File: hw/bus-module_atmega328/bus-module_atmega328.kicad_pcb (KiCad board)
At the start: 2 copper layers, 35 x 48 mm, 31 parts, among them J1 CONN_10X2, J2 CONN_7X2, J3 CONN-ISP-6, J5 CONN_1, J6 CONN_1, J7 CONN_1, J8 CONN_1, U1 ATMEGA328-TQFP32, U2 7,3728MHz, U3 25LC256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

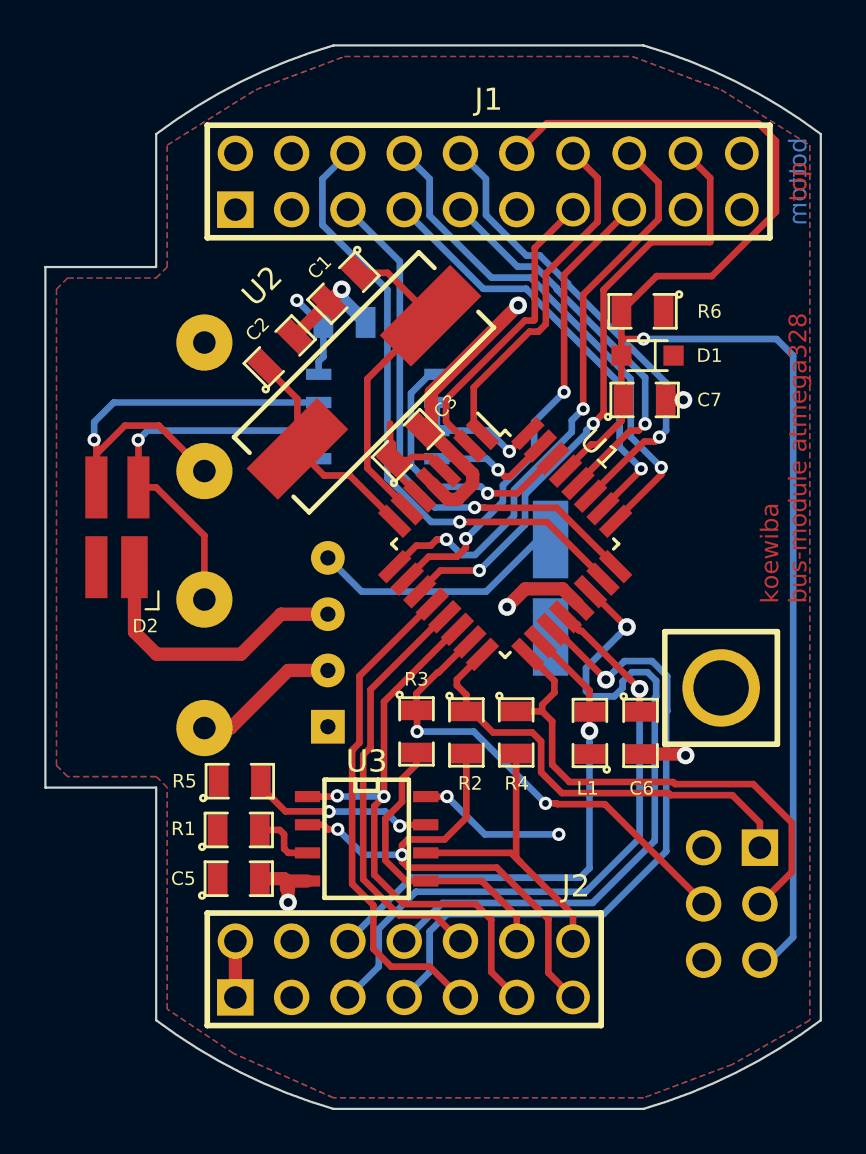
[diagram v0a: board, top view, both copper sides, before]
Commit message: bus-module_atmega328 update to rev B
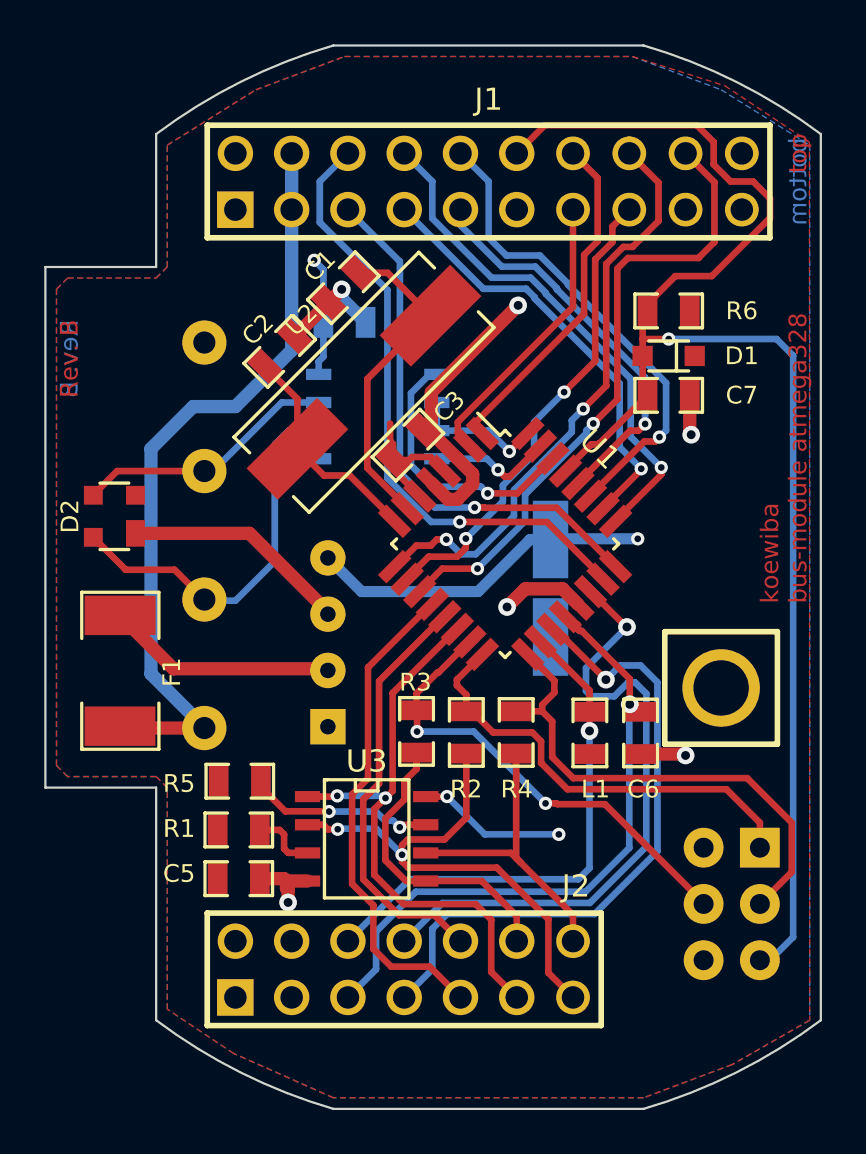
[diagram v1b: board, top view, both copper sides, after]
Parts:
- added F1: FUSE, Resistor:R_1812, F.Cu at (83.4, 104.2)
- C1, C2, C3, C5, C6, C7, C8: footprint Housings_SOIC:SM0805 -> Capacitors_SMD:C_0805
- C9: footprint Capacitors:cp_smd_6.3 -> Capacitors_SMD:CP_D6.3mm
- D1: footprint Diode:SOD323 -> Diode_SMD:D_SOD323
- D2: footprint Housings_SOT:SOT143R_Diode_Reverse -> Diode_SMD:D_SOT143
- J5, J6, J7, J8: footprint Connector_Miscelleaneus:WAGO243 -> Connector_WAGO:WAGO243
- L1: footprint Housings_SOIC:SM0805 -> Inductor:L_0805
- R1, R2, R3, R4, R5, R6: footprint Housings_SOIC:SM0805 -> Resistor:R_0805
- U2: footprint Crystal:HC49-SMD -> Crystal:CRY_HC49_SMD
- moved R6 1.18 mm to (108.1, 88.0)
- moved C7 1.11 mm to (108.1, 91.8)
- moved D1 0.96 mm to (108.1, 90.0)
- moved D2 0.52 mm to (83.1, 97.3), turned to 90 degrees
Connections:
- J1 pad 3: VCC -> +24V
- J1 pad 4: VCC -> +24V
- U5 pad 2: +24V -> Net-(F1-Pad1)
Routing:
- net +24V: track 6.65 -> 34.6 mm
- net Net-(F1-Pad1): track 0.00 -> 10.5 mm
- net /B: track 21.4 -> 11.9 mm, vias 1 -> 0
- net VCC: track 28.4 -> 34.4 mm, vias 3 -> 4
- net GND: track 44.2 -> 39.5 mm
- net //RESET: track 68.9 -> 66.6 mm
- net /ADC7: track 29.9 -> 28.3 mm
- net /ADC6: track 29.8 -> 28.6 mm
- net /AREF: track 29.8 -> 29.0 mm
- net /PD4: track 13.1 -> 12.5 mm
- net /PC4: track 20.8 -> 21.4 mm
- net /A: track 17.4 -> 17.7 mm, vias 1 -> 0
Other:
- rule trace_min: 0.3 -> 0.2
- board text added: "Rev. B"

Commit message: fixed silkscreen pinout description for 24V pins
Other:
- board text added: "GND 24V PC0 PC2 PC4 RESET PD3 PD5 PD7 nc"
- board text added: "GND 24V PC1 PC3 PC5 nc PD4 PD6 nc nc"
- board text removed: "GND VCC PC0 PC2 PC4 RESET PD3 PD5 PD7 nc"
- board text removed: "GND VCC PC1 PC3 PC5 nc PD4 PD6 nc nc"
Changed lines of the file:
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@@
   (title_block
     (title "bus-module atmega328")
-    (date 2018-09-22)
+    (date 2018-09-24)
     (rev B)
     (company KoeWiBa)
@@
     (effects (font (size 1 1) (thickness 0.15)) (justify mirror))
   )
-  (gr_text "GND\nVCC\nPC0\nPC2\nPC4\nRESET\nPD3\nPD5\nPD7\nnc" (at 106.2 88.49 90) (layer B.SilkS)
+  (gr_text "GND\n24V\nPC0\nPC2\nPC4\nRESET\nPD3\nPD5\nPD7\nnc" (at 106.2 88.11 90) (layer B.SilkS)
     (effects (font (size 0.8 0.8) (thickness 0.15)) (justify right mirror))
   )
@@
     (effects (font (size 1 1) (thickness 0.15)) (justify mirror))
   )
-  (gr_text "GND\nVCC\nPC1\nPC3\nPC5\nnc\nPD4\nPD6\nnc\nnc" (at 106.2 89.125 90) (layer B.SilkS)
+  (gr_text "GND\n24V\nPC1\nPC3\nPC5\nnc\nPD4\nPD6\nnc\nnc" (at 106.175 88.81 90) (layer B.SilkS)
     (effects (font (size 0.8 0.8) (thickness 0.15)) (justify left mirror))
   )
